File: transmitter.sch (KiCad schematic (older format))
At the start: 55 parts

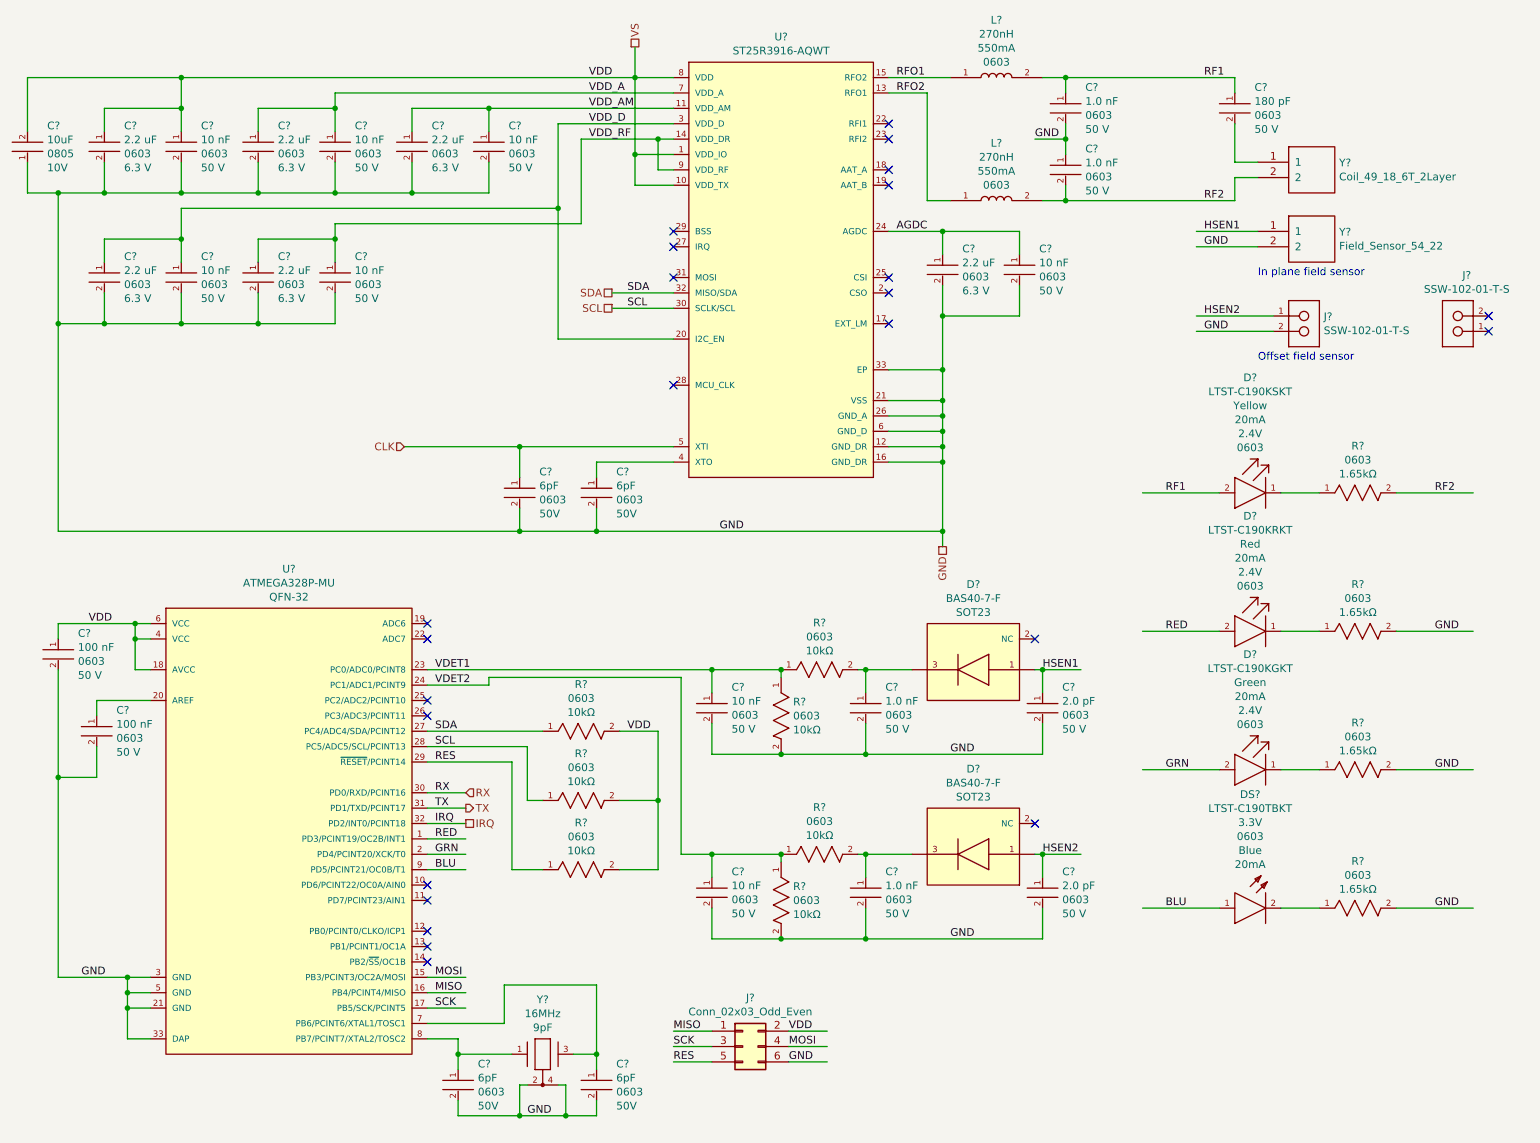
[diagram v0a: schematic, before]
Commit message: add si5351. and separate power side logic SCLP SDAP and IRQP when power not applied to +5VP.
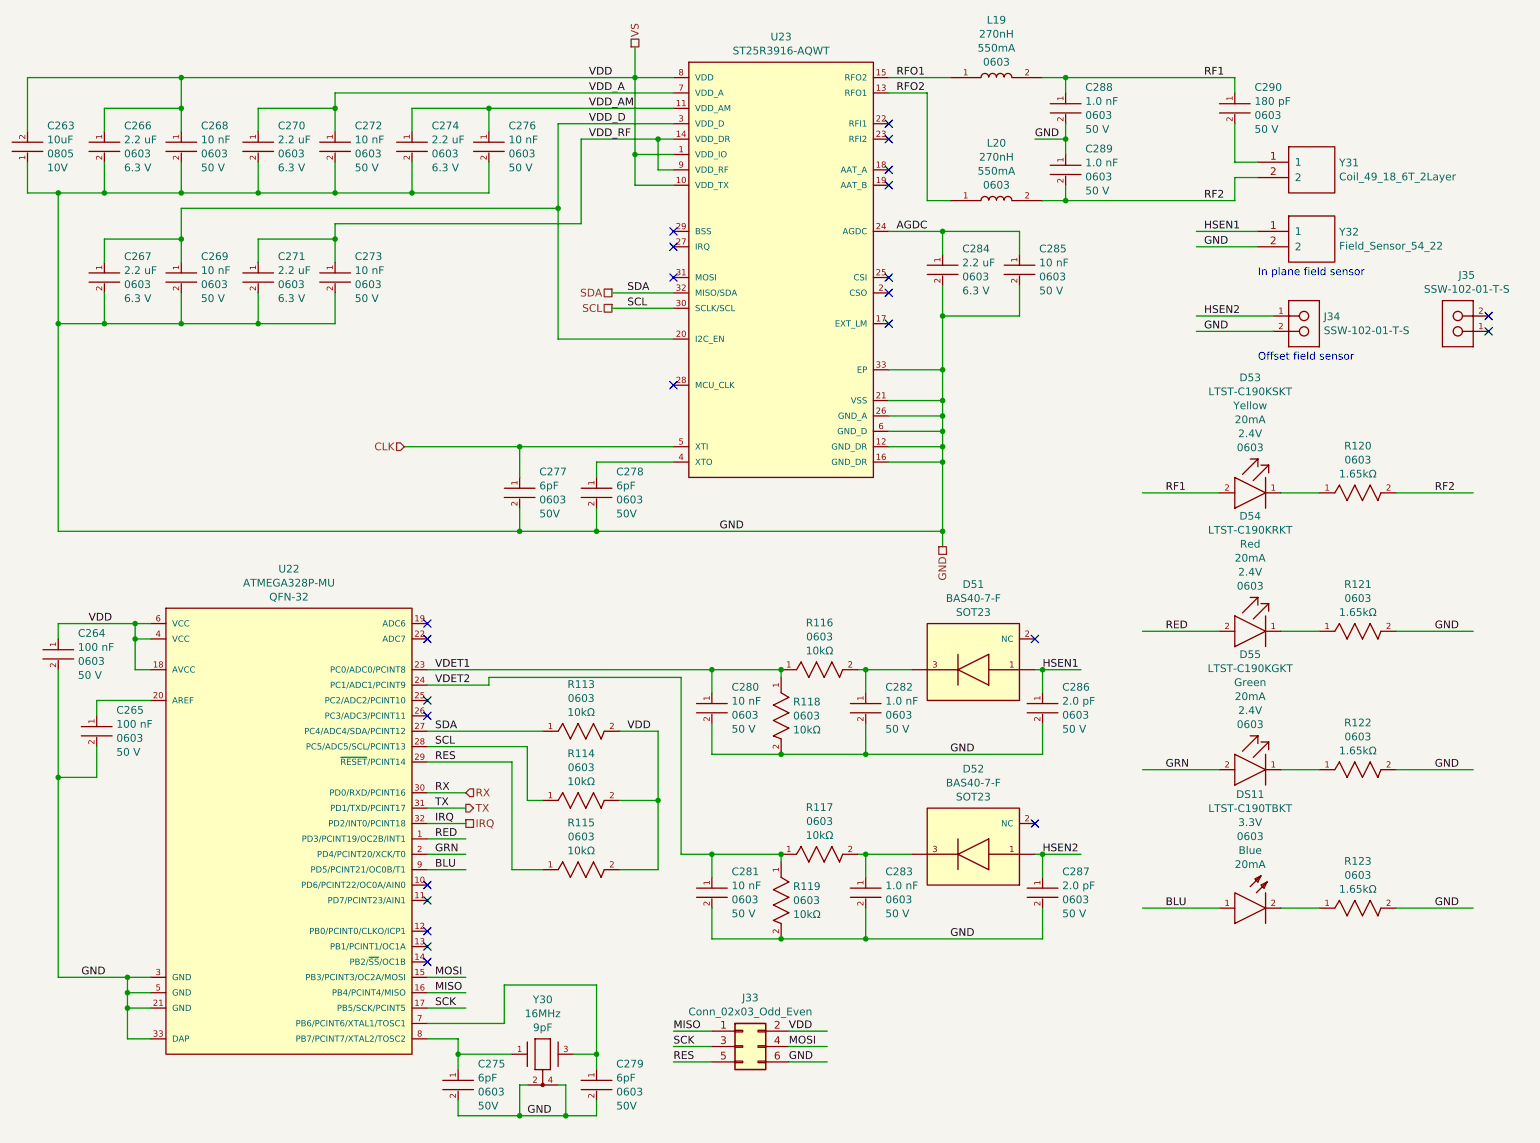
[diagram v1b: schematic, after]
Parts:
- gave numbers to parts that had none: 55

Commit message: update
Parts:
- renumbered D9 to D10, D10 to D11, DS2 to D12, D6 to D7, D7 to D8, D8 to D9, R14 to R20, R15 to R21, R16 to R22, R17 to R23, R18 to R24, R19 to R25, R20 to R26, R21 to R27, R22 to R28, R23 to R29, R24 to R30

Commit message: update
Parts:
- C11: footprint YAGEO-CC0805-0-0-* -> project:YAGEO-CC0805-0-0-0
- C135, C139, C25, C26: footprint TDK-CGA3E-0.3-0.1-0-0-* -> project:TDK-CGA3E-0.3-0.1-0-0-IPC_A
- C14, C15, C16, C17, C18, C19, C20, C21, C22, C24, C28, C29, C30, C31, C32, C33, C36, C37, C38: footprint YAGEO-CC0603-DA-05_2018-24-* -> project:YAGEO-CC0603-0-0-0
- C34, C35: footprint KEMET-C0603C-CF-0-0-* -> project:KEMET-C0603C-CF-0-0-MFG
- D10: footprint Lite-On-LTST-C190KRKT-* -> project:Lite-On-LTST-C190KRKT-MFG
- D11: footprint Lite-On-LTST-C190KGKT-* -> project:Lite-On-LTST-C190KGKT-MFG
- D12: footprint Vishay_Lite-On-LTST-C190TBKT-* -> project:Vishay_Lite-On-LTST-C190TBKT-Manufacturer_Recommended
- D7, D8: footprint Diodes_Inc.-SOT23-01_2017-0-* -> project:Diodes_Inc.-SOT23-01_2017-0-MFG
- D9: footprint Lite-On-LTST-C190KSKT-* -> project:Lite-On-LTST-C190KSKT-MFG
- J18: footprint (none) -> Pin_Headers:Pin_Header_Straight_2x03_Pitch2.54mm
- L1, L2: footprint INDC1608X95N -> project:INDC1608X95N
- R20, R21, R22, R23, R24, R25, R26, R27, R28, R29, R30: footprint Yageo-RC0603-0-0-* -> project:Yageo-RC0603-0-0-IPC_A
- U12: footprint Microchip___Atmel-ATMEGA328P-MU-* -> project:Microchip___Atmel-ATMEGA328P-MU-Level_A
- U5: footprint STMicroelectronics-VFQFPN32-B04R-0-1-* -> project:STMicroelectronics-VFQFPN32-B04R-0-1-IPC_A
- Y15: footprint Epson-TSX-3225_16.0000MF09Z-AC3-* -> project:Epson-TSX-3225_16.0000MF09Z-AC3-0
- Y4: footprint NFCPower:Coil_49_18_6T_2Layer -> project:Coil_49_18_6T_2Layer

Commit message: initial placement
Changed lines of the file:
@@
 VDD_RF
 Text Label 6400 1050 0    50   ~ 0
+RFO2
+Text Label 6400 1150 0    50   ~ 0
 RFO1
-Text Label 6400 1150 0    50   ~ 0
-RFO2
 Text Label 8400 1050 0    50   ~ 0
+RF2
+Text Label 8400 1850 0    50   ~ 0
 RF1
-Text Label 8400 1850 0    50   ~ 0
-RF2
 Text Label 6400 2050 0    50   ~ 0
 AGDC

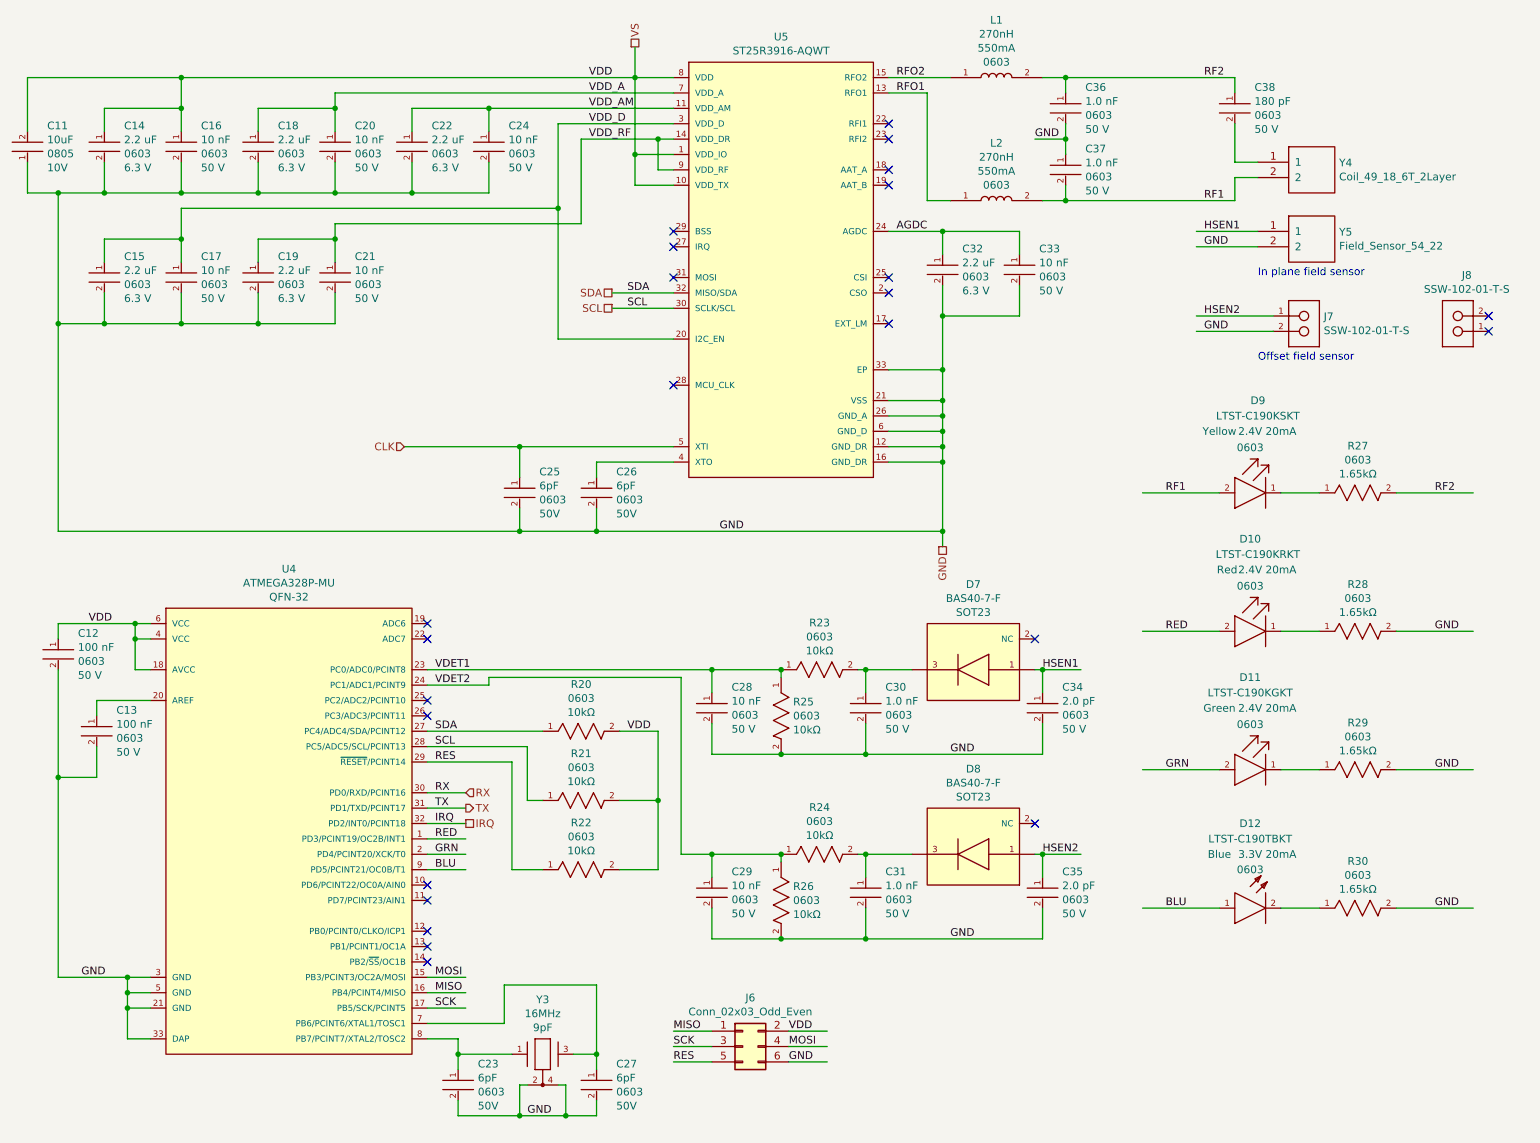
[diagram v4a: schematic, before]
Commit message: continue routing. add INA219 to monitor +5VP rail.
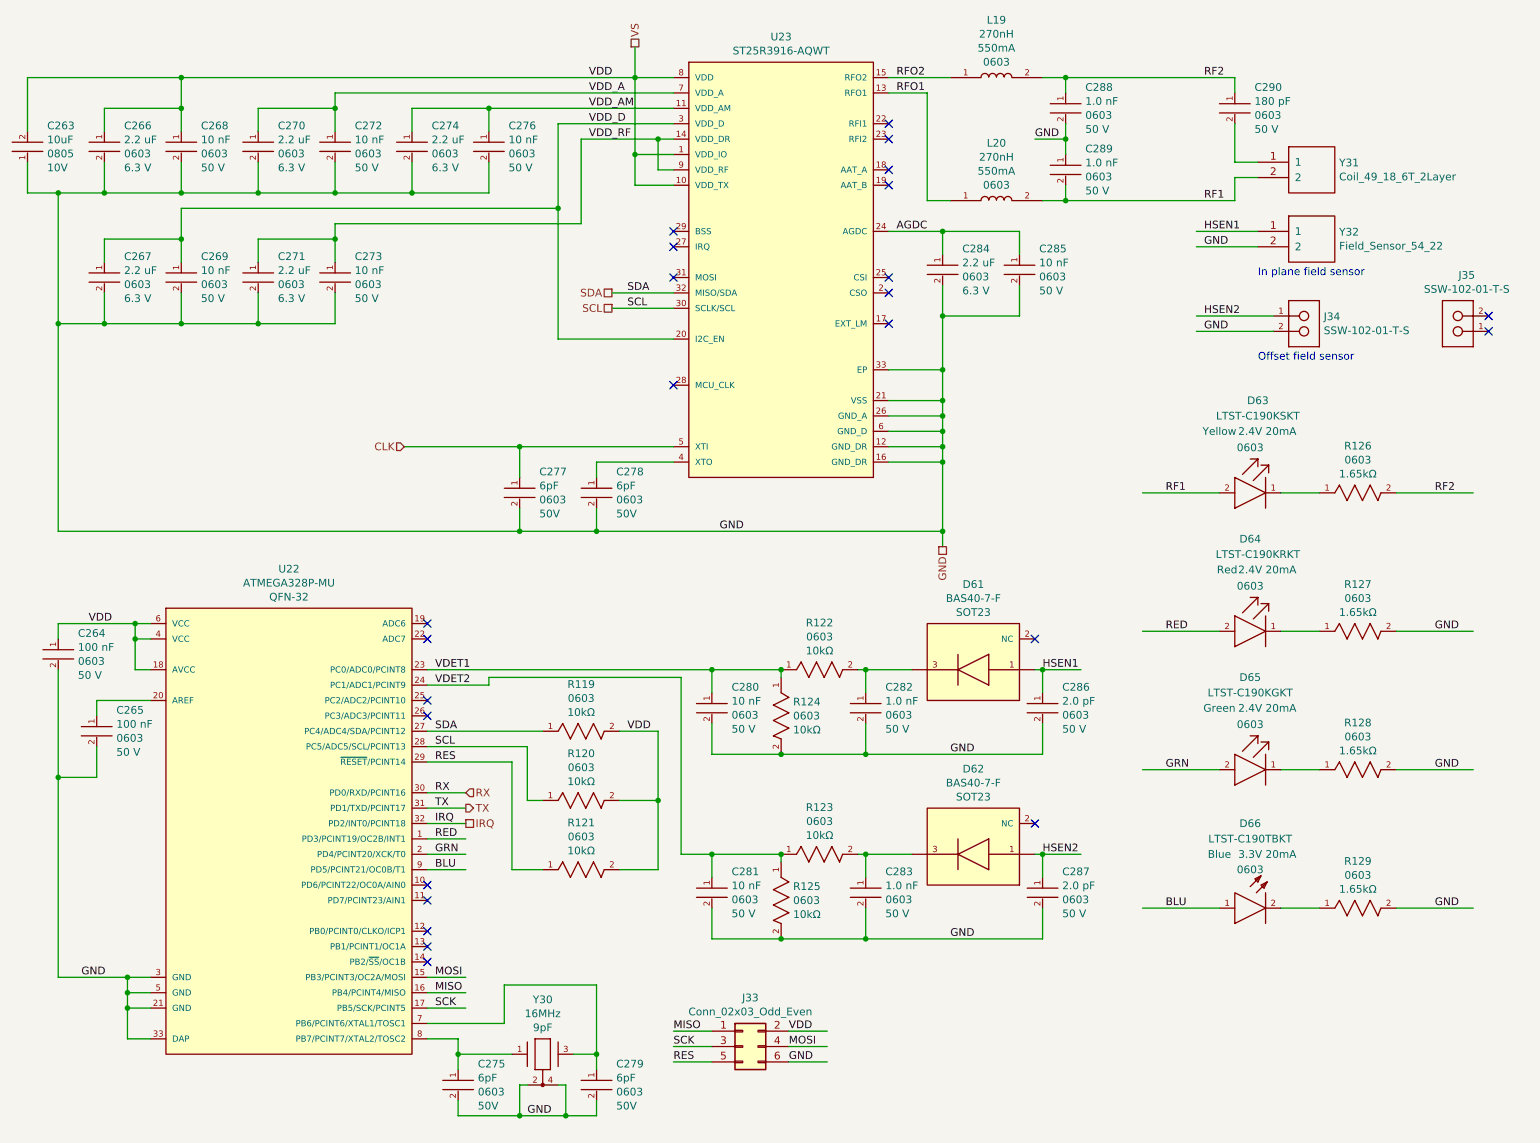
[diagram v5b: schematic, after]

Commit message: rev 2
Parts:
- removed C28, C29: CC0603KRX7R9BB103, project:YAGEO-CC0603-0-0-0, symbol project:CC0603KRX7R9BB103
- removed J7: SSW-102-01-T-S, project:Samtec-SSW-102-01-T-S-Manufacturer_Recommended, symbol project:SSW-102-01-T-S
- removed R24, R26: RC0603FR-0710KL, project:Yageo-RC0603-0-0-IPC_A, symbol project:RC0603FR-0710KL
- added C28: CC0603KRX7R6BB224, project:YAGEO-CC0603-0-0-0, symbol project:CC0603KRX7R6BB224
- added C29, C40: CC0603KRX7R7BB105, project:YAGEO-CC0603-0-0-0, symbol project:CC0603KRX7R7BB105
- added J7: SSW-104-01-T-S, project:Samtec-SSW-104-01-T-S-Manufacturer_Recommended, symbol project:SSW-104-01-T-S
- added R24, R6: RC0603FR-071K65L, project:Yageo-RC0603-0-0-IPC_A, symbol project:RC0603FR-071K65L
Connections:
- net labels added: A0, A1, A2, A3, LSEN2, VPD2
- wire segments 235 -> 248
- no-connect marks 24 -> 19
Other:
- note added: "Offset field and light sensor"
- note removed: "Offset field sensor"
- moved on the sheet: R20, R21, R22
